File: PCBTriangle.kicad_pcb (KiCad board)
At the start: 2 copper layers, 100 x 100 mm, 18 parts

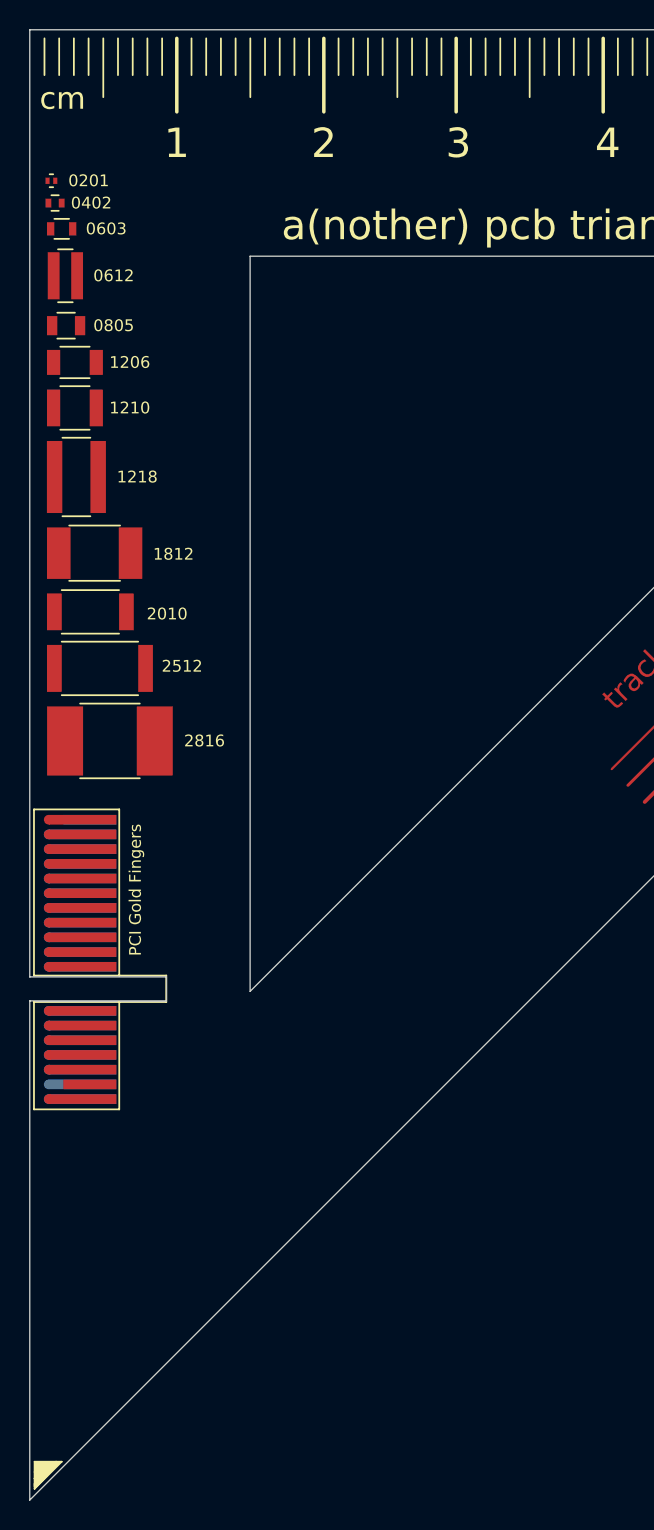
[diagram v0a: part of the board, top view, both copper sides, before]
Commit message: Added Through Hole Vias
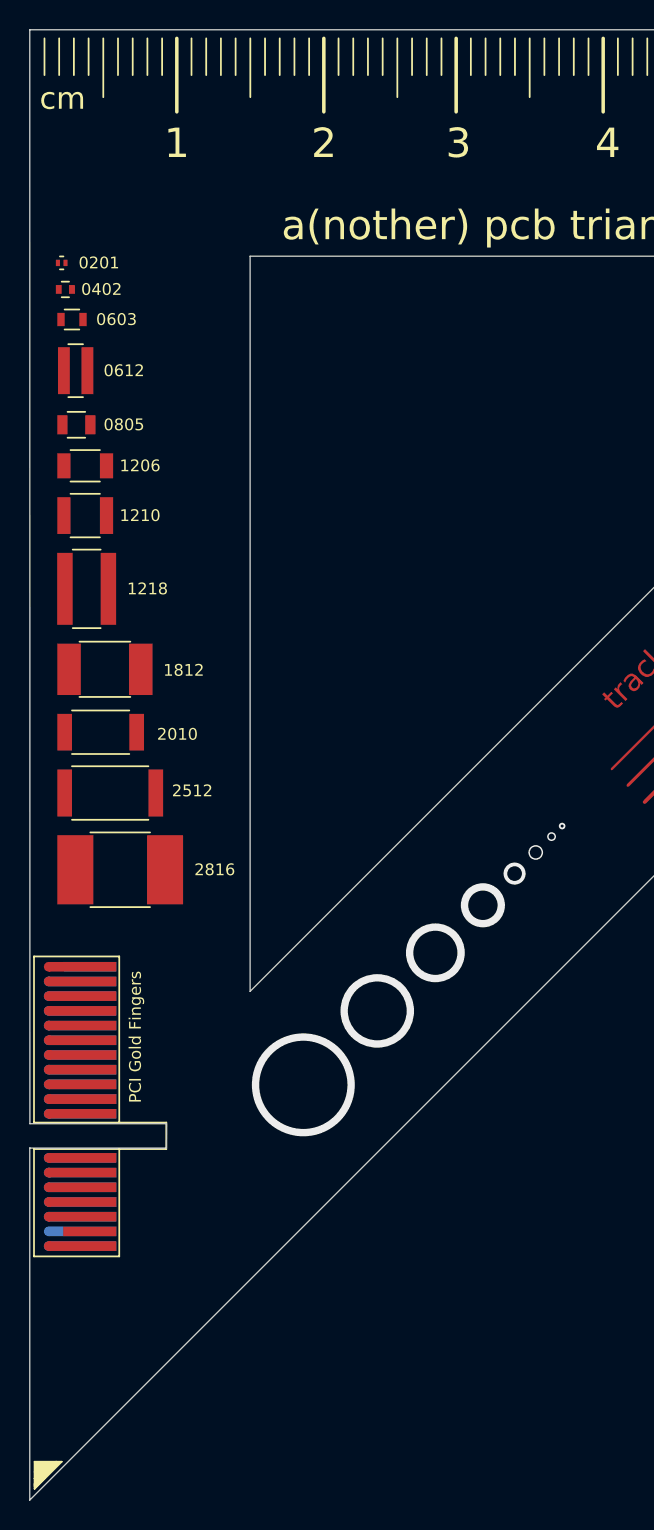
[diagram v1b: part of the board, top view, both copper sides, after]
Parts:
- moved PCI Gold Fingers 10.0 mm to (87.2, 108.8)
- moved 2816 8.79 mm to (89.3, 102.2)
- moved 2512 8.50 mm to (88.6, 97.0)
- moved 2010 8.22 mm to (87.9, 92.9)
- moved 1812 7.93 mm to (88.2, 88.6)
- moved 1218 7.64 mm to (87.0, 83.1)
- moved 1210 7.35 mm to (86.9, 78.1)
- moved 1206 7.07 mm to (86.9, 74.8)
- moved 0805 6.78 mm to (86.3, 72.0)
- moved 0612 6.49 mm to (86.2, 68.3)
- moved 0603 6.20 mm to (86.0, 64.8)
- moved 0402 5.92 mm to (85.5, 62.8)
- moved 0201 5.63 mm to (85.3, 61.0)
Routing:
- net (no net): vias 0 -> 8
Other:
- outline, holes or cut-outs redrawn
- net class Default: clearance 0.2 -> 0.127; trace_width 0.25 -> 0.127; via_dia 0.8 -> 0.4; via_drill 0.4 -> 0.2
- rule trace_clearance: 0.2 -> 0.127
- rule trace_min: 0.2 -> 0.127
- rule via_min_drill: 0.3 -> 0.2

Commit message: updated silkscreen
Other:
- board text added: "0.4/0.2"
- board text added: "0.6/0.4"
- board text added: "1.0/0.8"
- board text added: "1.5/1"
- board text added: "3.0/2.0"
- board text added: "4.0/3/0"
- board text added: "5.0/4.0"
- board text added: "7.0/6.0"
- board text added: "hole/drl (mm)"
